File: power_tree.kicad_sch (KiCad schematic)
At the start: 4 parts, among them U3 LM1117MP-3.3

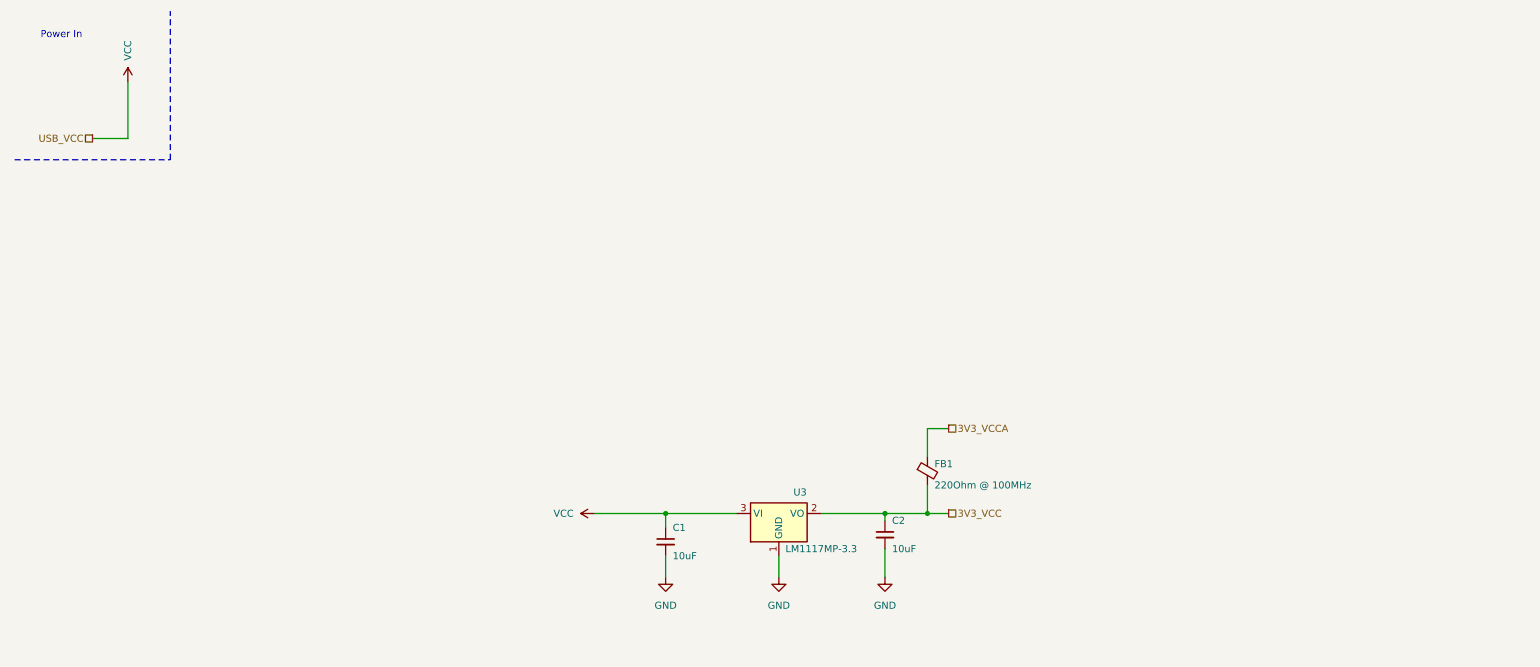
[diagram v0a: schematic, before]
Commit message: fix(Power_led): Moved the power led to power tree sheet from USB UART sheet
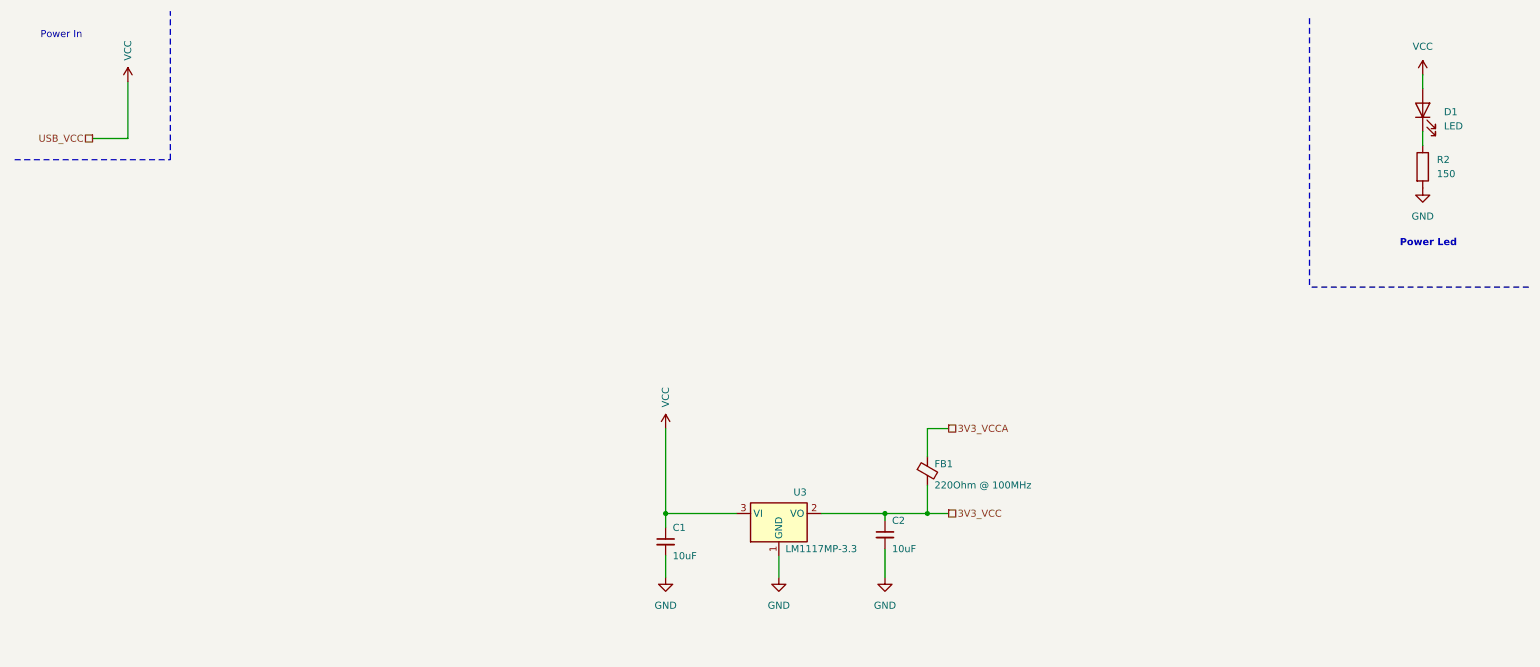
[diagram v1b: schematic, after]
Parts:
- added D1: LED, LED_SMD:LED_0603_1608Metric_Pad1.05x0.95mm_HandSolder, symbol Device:LED
- added R2: 150, Resistor_SMD:R_0603_1608Metric_Pad0.98x0.95mm_HandSolder, symbol Device:R
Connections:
- net GND: now also R2.2
- net VCC: now also D1.2 (A)
- new net: D1.1 (K), R2.1
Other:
- note added: "Power Led"

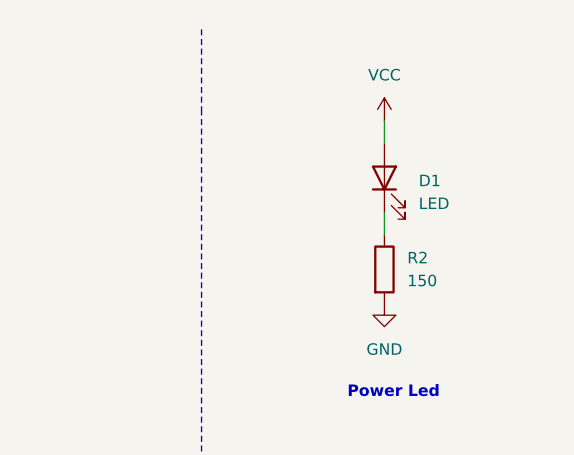
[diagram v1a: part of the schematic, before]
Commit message: feat(POWER_LED): Changed the position of the power led to the beginning of the power tree
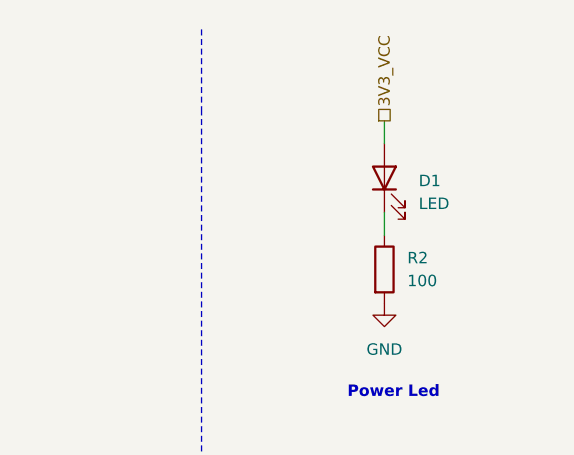
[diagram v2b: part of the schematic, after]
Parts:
- R2: value 150 -> 100
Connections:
- net 3V3_VCC: now also D1.2 (A)
- net VCC: no longer D1.2 (A)
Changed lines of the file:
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@@
+	(hierarchical_label "3V3_VCC"
+		(shape passive)
+		(at 265.43 22.86 90)
+		(effects
+			(font
+				(size 1.27 1.27)
+			)
+			(justify left)
+		)
+	)
 	(hierarchical_label "3V3_VCC"
 		(shape passive)
@@
 			)
 		)
-		(property "Value" "150"
+		(property "Value" "100"
 			(at 267.97 40.6399 0)
 			(effects
@@
 					(unit 1)
 				)
-			)
-		)
-	)
-	(symbol
-		(lib_id "power:VCC")
-		(at 265.43 22.86 0)
-		(unit 1)
-		(exclude_from_sim no)
-		(in_bom yes)
-		(on_board yes)
-		(dnp no)
-		(fields_autoplaced yes)
-		(property "Reference" "#PWR036"
-			(at 265.43 26.67 0)
-			(effects
-				(font
-					(size 1.27 1.27)
-				)
-				(hide yes)
-			)
-		)
-		(property "Value" "VCC"
-			(at 265.43 17.78 0)
-			(effects
-				(font
-					(size 1.27 1.27)
-				)
-			)
-		)
-		(property "Footprint" ""
-			(at 265.43 22.86 0)
-			(effects
-				(font
-					(size 1.27 1.27)
-				)
-				(hide yes)
-			)
-		)
-		(property "Datasheet" ""
-			(at 265.43 22.86 0)
-			(effects
-				(font
-					(size 1.27 1.27)
-				)
-				(hide yes)
-			)
-		)
-		(property "Description" "Power symbol creates a global label with name \"VCC\""
-			(at 265.43 22.86 0)
-			(effects
-				(font
-					(size 1.27 1.27)
-				)
-				(hide yes)
-			)
-		)
-		(pin "1"
-		)
-		(instances
-			(project "HW"
-				(path "/01550cd7-b424-469c-925b-c370f3609cd4/360b299b-84d8-4d26-8110-4c6e53cc9fa4"
-					(reference "#PWR036")
-					(unit 1)
-				)

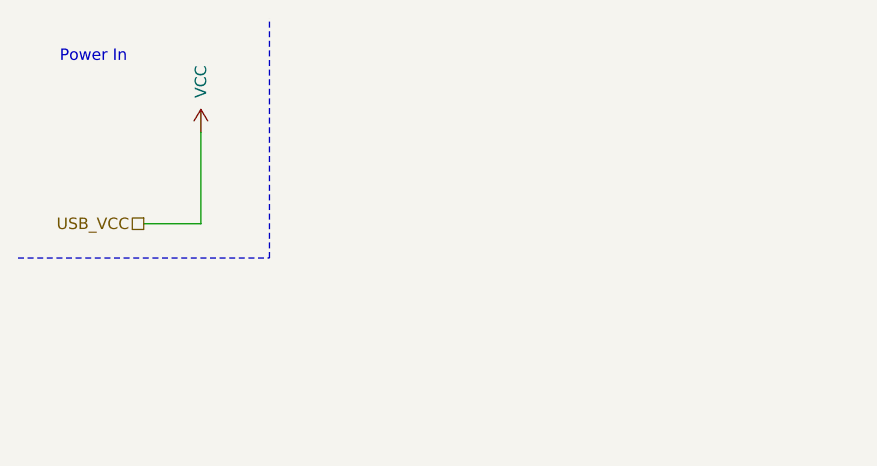
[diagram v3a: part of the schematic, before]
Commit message: fix: moved some power flags to the power tree page
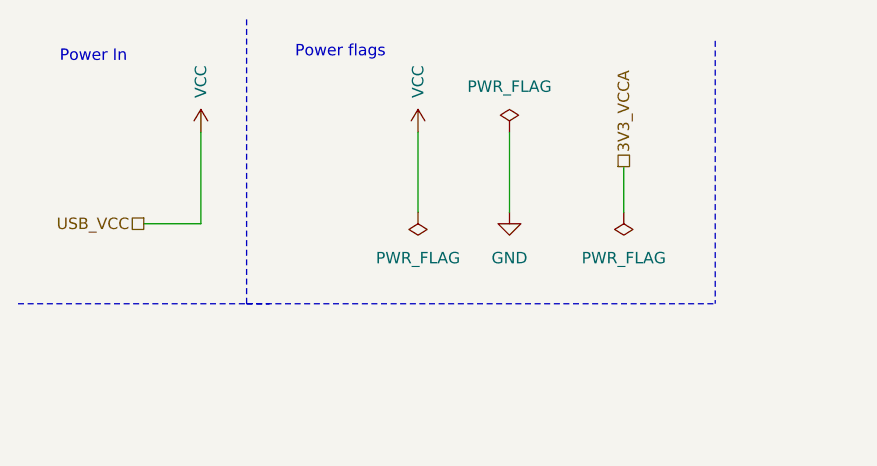
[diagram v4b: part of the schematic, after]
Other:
- note added: "Power flags"

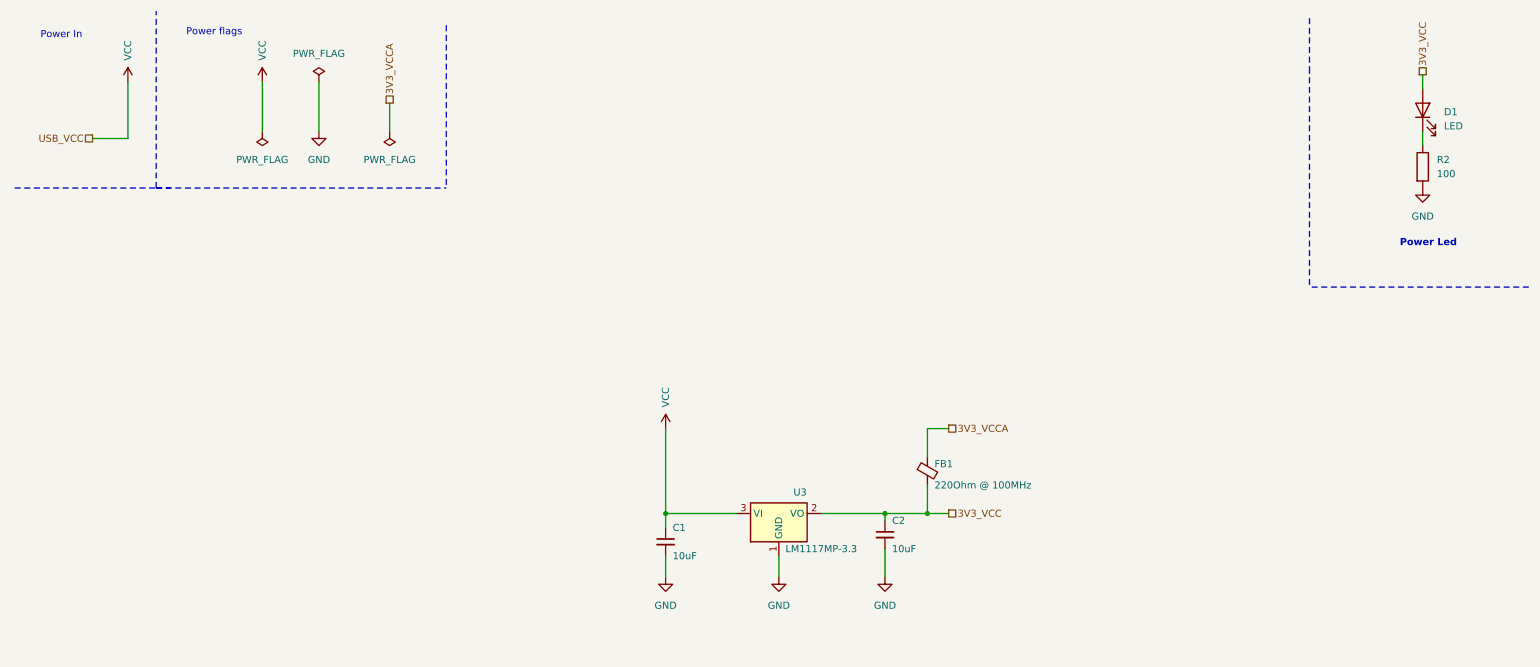
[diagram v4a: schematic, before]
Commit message: feat(power): redesign power tree with explicit +3.3V/+5V/+3.3VA rails
Replaces the generic power:VCC symbols with explicit rails (+3.3V, +5V, +3.3VA) to make the regulator topology unambiguous in the power tree. Restructures U3 (LM1117MP-3.3), C1, R2, FB1, D1, and the PWR_FLAG placements around the new rails, and drops the now-redundant 3V3_VCCA, 3V3_VCC, and USB_VCC hierarchical labels in favour of the power symbols themselves.
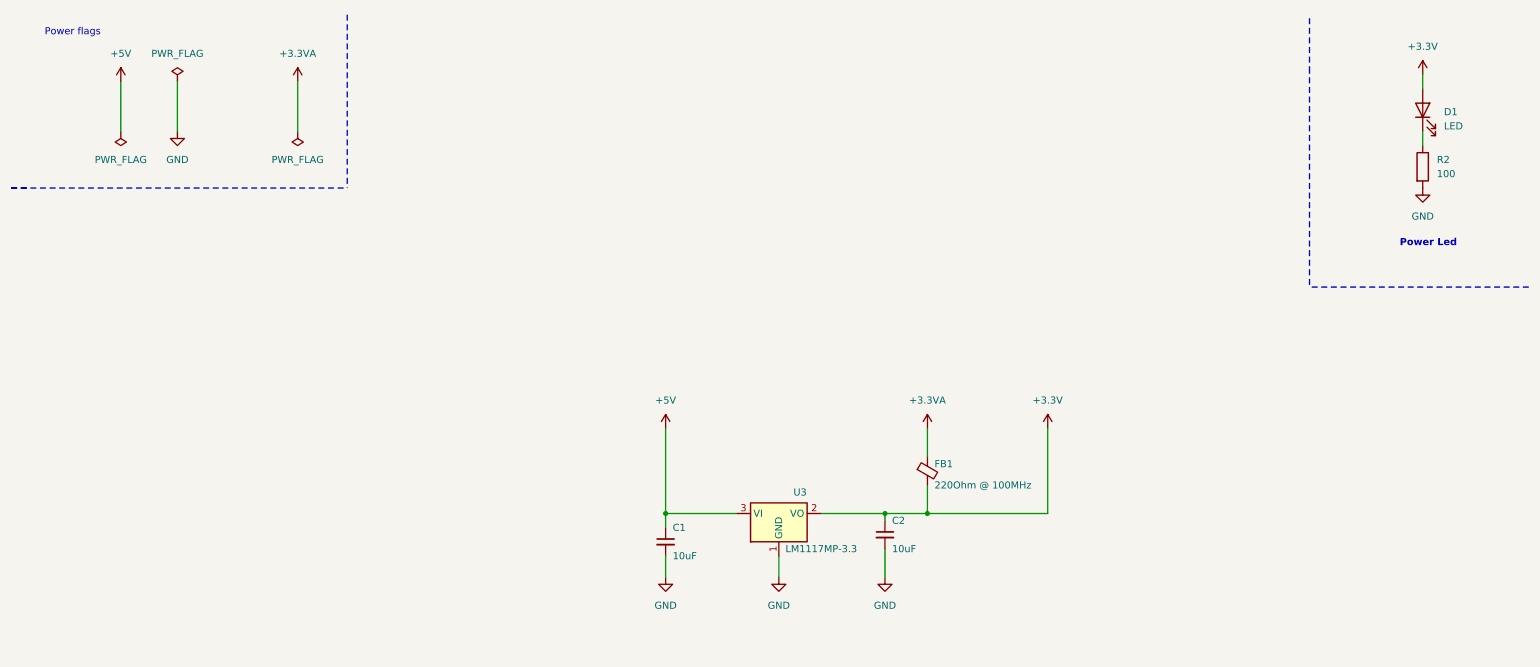
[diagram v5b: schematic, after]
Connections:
- net 3V3_VCC renamed +3.3V
- net 3V3_VCCA renamed +3.3VA
- net VCC renamed +5V
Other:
- note removed: "Power In"

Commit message: Added new 3.3V LDO power tree with load sharing
- Added AP2112K-3.3 LDO to run directly from the battery or from the usb.
- Implemented a P-Channel MOSFET and Schottky diode power mux for safe load sharing.
- Implemented a TP4056 based circuit to charge the battery.
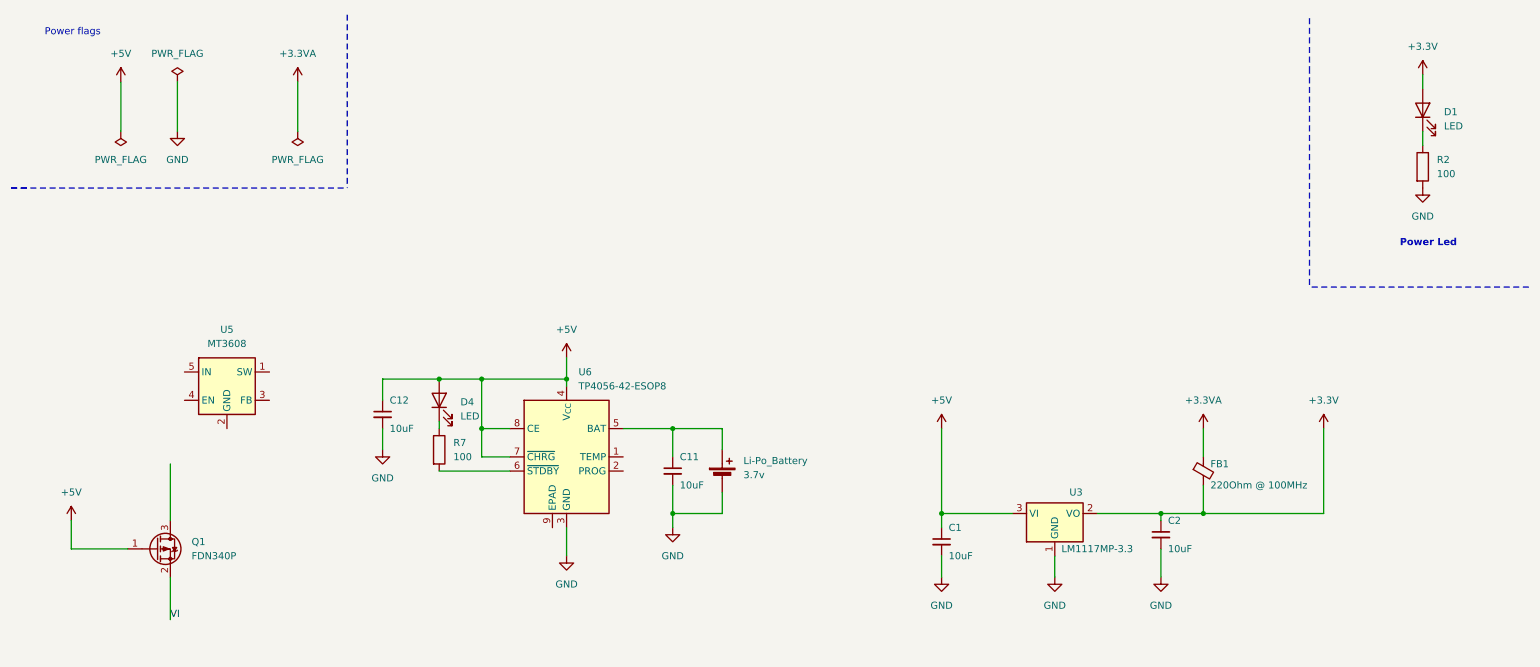
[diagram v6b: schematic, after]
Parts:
- added C11, C12: 10uF, Capacitor_SMD:C_0603_1608Metric_Pad1.08x0.95mm_HandSolder, symbol Device:C_Small
- added D4: LED, LED_SMD:LED_0603_1608Metric_Pad1.05x0.95mm_HandSolder, symbol Device:LED
- added Li-Po_Battery: 3.7v, symbol Device:Battery_Cell
- added Q1: FDN340P, Package_TO_SOT_SMD:SOT-23, symbol Transistor_FET:FDN340P
- added R7: 100, Resistor_SMD:R_0603_1608Metric_Pad0.98x0.95mm_HandSolder, symbol Device:R
- added U5: MT3608, Package_TO_SOT_SMD:SOT-23-6, symbol Regulator_Switching:MT3608
- added U6: TP4056-42-ESOP8, Package_SO:SOIC-8-1EP_3.9x4.9mm_P1.27mm_EP2.41x3.3mm_ThermalVias, symbol Battery_Management:TP4056-42-ESOP8
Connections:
- net +5V: now also C12.1, D4.2 (A), Q1.1 (G), U6.4 (V_{CC}), U6.7 (~{CHRG}), U6.8 (CE)
- net GND: now also C11.2, C12.2, Li-Po_Battery.2 (-), U6.3 (GND)
- new net: D4.1 (K), R7.1
- new net: C11.1, Li-Po_Battery.1 (+), U6.5 (BAT)
- new net: R7.2, U6.6 (~{STDBY})
- new net VI: Q1.2 (S)
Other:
- moved on the sheet: C1, C2, FB1, U3

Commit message: Fix: resolved DRC errors
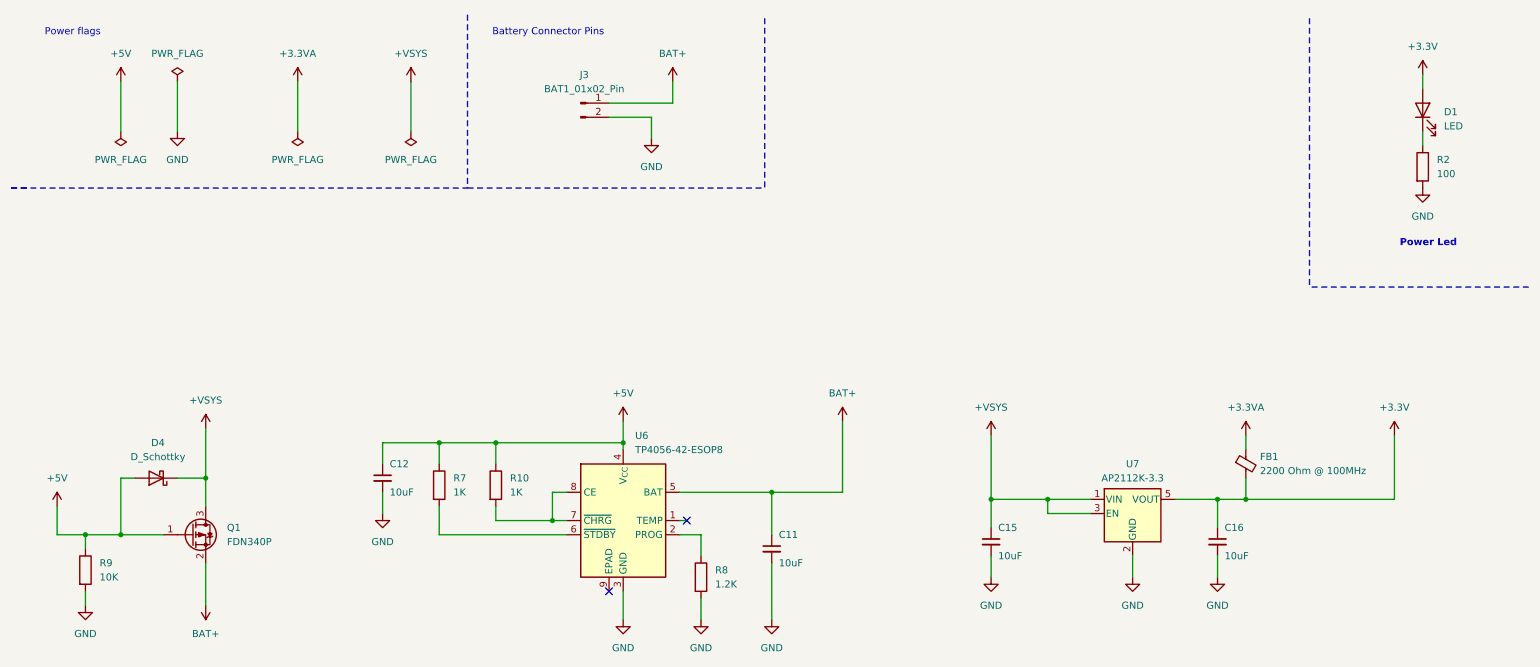
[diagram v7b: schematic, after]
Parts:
- removed C1, C2: 10uF, Capacitor_SMD:C_0603_1608Metric_Pad1.08x0.95mm_HandSolder, symbol Device:C_Small
- removed D4: LED, LED_SMD:LED_0603_1608Metric_Pad1.05x0.95mm_HandSolder, symbol Device:LED
- removed Li-Po_Battery: 3.7v, symbol Device:Battery_Cell
- removed U3: LM1117MP-3.3, Package_TO_SOT_SMD:SOT-223-3_TabPin2, symbol Regulator_Linear:LM1117MP-3.3
- removed U5: MT3608, Package_TO_SOT_SMD:SOT-23-6, symbol Regulator_Switching:MT3608
- added C15, C16: 10uF, Capacitor_SMD:C_0603_1608Metric_Pad1.08x0.95mm_HandSolder, symbol Device:C_Small
- added D4: D_Schottky, Diode_SMD:D_SOD-123, symbol Device:D_Schottky
- added J3: BAT1_01x02_Pin, Connector_JST:JST_PH_S2B-PH-K_1x02_P2.00mm_Horizontal, symbol Connector:Conn_01x02_Pin
- added R10: 1K, Resistor_SMD:R_0603_1608Metric_Pad0.98x0.95mm_HandSolder, symbol Device:R
- added R8: 1.2K, Resistor_SMD:R_0603_1608Metric_Pad0.98x0.95mm_HandSolder, symbol Device:R
- added R9: 10K, Resistor_SMD:R_0603_1608Metric_Pad0.98x0.95mm_HandSolder, symbol Device:R
- added U7: AP2112K-3.3, Package_TO_SOT_SMD:SOT-23-5, symbol Regulator_Linear:AP2112K-3.3
- FB1: value 220Ohm @ 100MHz -> 2200 Ohm @ 100MHz
- R7: value 100 -> 1K
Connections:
- net VI is gone; now on net BAT+: Q1.2 (S)
- net +3.3V: now also C16.1, U7.5 (VOUT)
- net +5V: now also R7.1, D4.2 (A), R10.1, R9.1; no longer U6.7 (~{CHRG}), U6.8 (CE)
- net GND: now also C15.2, C16.2, J3.2 (Pin_2), R8.2, R9.2, U7.2 (GND)
- net at U6.2 (PROG): now also R8.1
- net BAT+: now reaches C11.1, U6.5 (BAT)
- net BAT+: now also J3.1 (Pin_1)
- net +VSYS: now reaches Q1.3 (D)
- net +VSYS: now also C15.1, D4.1 (K), U7.1 (VIN), U7.3 (EN)
- new net: R10.2, U6.7 (~{CHRG}), U6.8 (CE)
- no-connect marks 0 -> 2
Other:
- note added: "Battery Connector Pins"
- moved on the sheet: C11, C12, Q1, R7, U6
